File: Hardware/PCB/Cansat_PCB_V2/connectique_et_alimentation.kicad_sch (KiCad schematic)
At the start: 40 parts, among them IC1 Alim STM Baro GPS IMU, IC2 Alim LoRa, J10 Connecteur IHM, J2 Connecteur Batterie, J3 Connecteur STLINK, J4 Connecteur Moteur, J5 Connecteur TOF, J6 Connecteur GPS, J7 Connecteur LoRa, J9 Connecteur IHM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

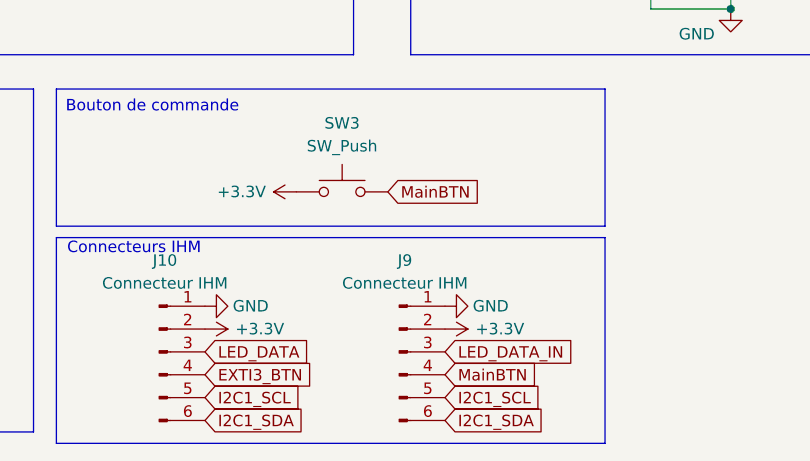
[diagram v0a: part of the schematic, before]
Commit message: ajout du connecteur IHM dans l'éditeur de PCB
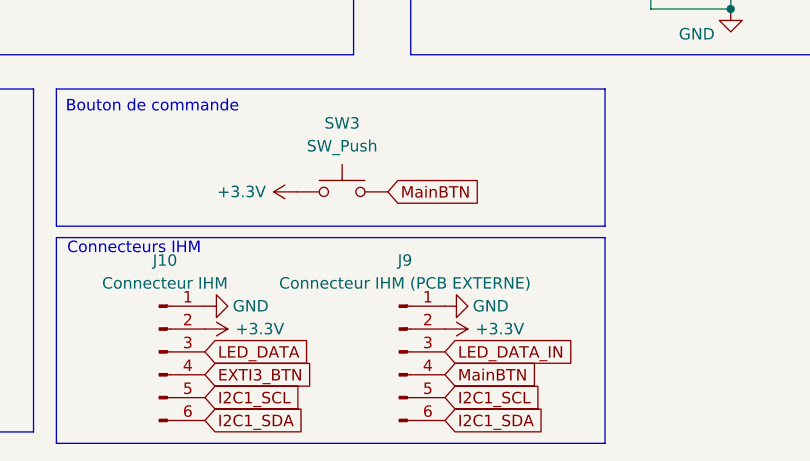
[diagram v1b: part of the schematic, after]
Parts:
- J10: footprint (none) -> Connector_JST:JST_SH_BM06B-SRSS-TB_1x06-1MP_P1.00mm_Vertical
- J9: value Connecteur IHM -> Connecteur IHM (PCB EXTERNE); footprint (none) -> Connector_JST:JST_SH_BM06B-SRSS-TB_1x06-1MP_P1.00mm_Vertical
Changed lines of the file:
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@@
 			)
 		)
-		(property "Footprint" ""
+		(property "Footprint" "Connector_JST:JST_SH_BM06B-SRSS-TB_1x06-1MP_P1.00mm_Vertical"
 			(at 124.46 186.69 0)
 			(effects
@@
 			)
 		)
-		(property "Value" "Connecteur IHM"
+		(property "Value" "Connecteur IHM (PCB EXTERNE)"
 			(at 151.765 179.07 0)
 			(effects
@@
 			)
 		)
-		(property "Footprint" ""
+		(property "Footprint" "Connector_JST:JST_SH_BM06B-SRSS-TB_1x06-1MP_P1.00mm_Vertical"
 			(at 151.13 186.69 0)
 			(effects

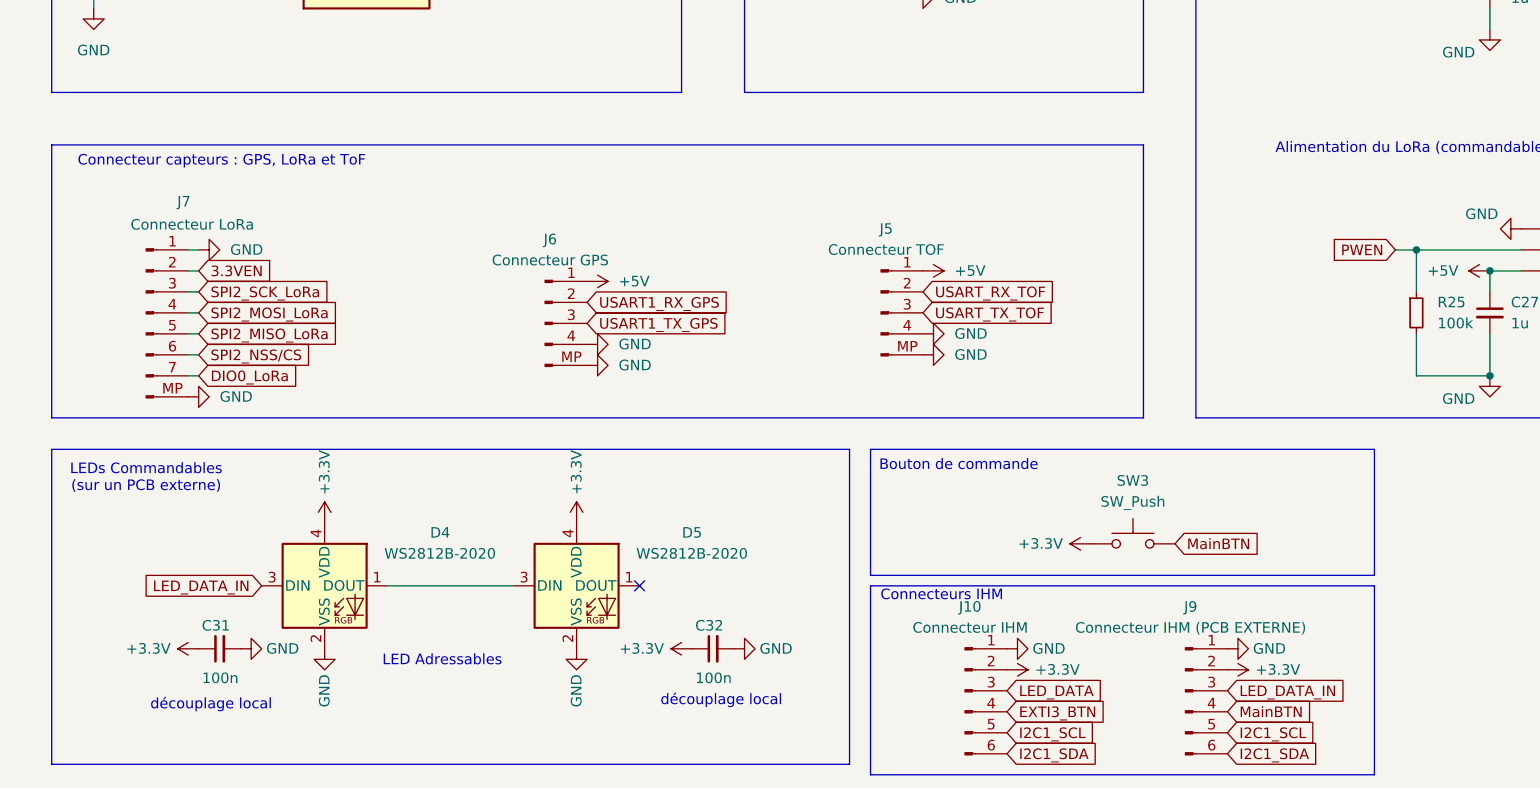
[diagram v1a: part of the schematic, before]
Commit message: Conn Camera 2 pins et deplacement du transistor dans un pcb intermédiaire
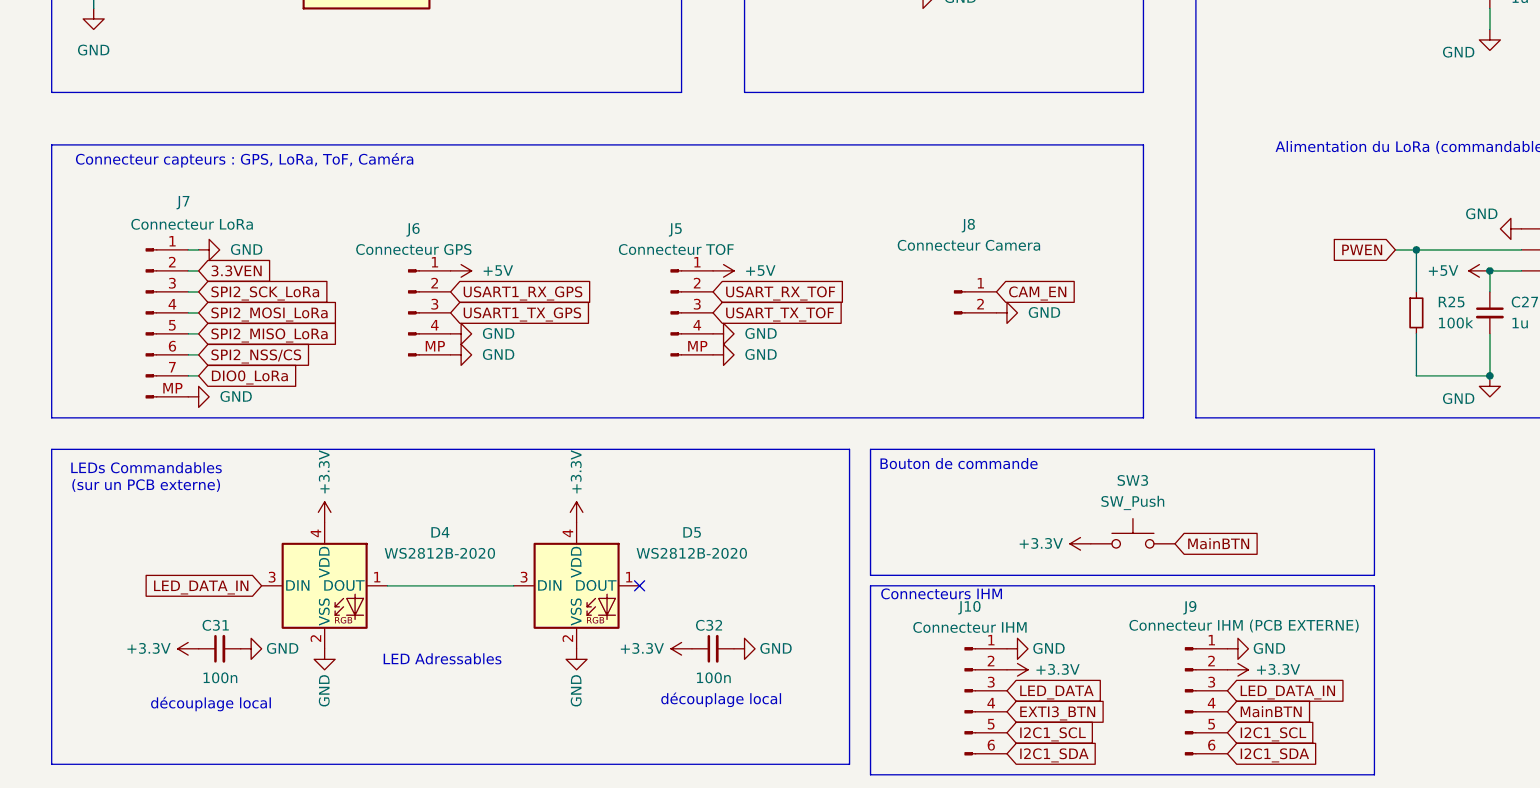
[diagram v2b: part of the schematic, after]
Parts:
- added J8: Connecteur Camera, Connector_JST:JST_SH_BM02B-SRSS-TB_1x02-1MP_P1.00mm_Vertical, symbol Connector:Conn_01x02_Pin
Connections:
- net GND: now also J8.2 (Pin_2)
- new net CAM_EN: J8.1 (Pin_1)
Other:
- note added: "Connecteur capteurs : GPS, LoRa, ToF, Caméra"
- note removed: "Connecteur capteurs : GPS, LoRa et ToF"
- moved on the sheet: J5, J6
